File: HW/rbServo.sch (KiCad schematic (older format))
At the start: 8 parts, among them P101 EXTCON, P104 p5V, P105 pGND, P109 pA, P113 M+, P114 M-

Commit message: Trying new layout
Signed-off-by: RasmusB <RasmusB@users.noreply.github.com>
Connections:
- net CAN_HIGH: now also P101.3 (P3); no longer P101.2 (P2)
- net CAN_LOW: now also P101.2 (P2); no longer P101.3 (P3)
- net GND: now also P101.4 (P4); no longer P101.1 (P1)
- net uIn: now also P101.1 (P1); no longer P101.4 (P4)
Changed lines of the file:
@@
 F 3 "" H 3800 3550 60  0001 C CNN
 	1    3800 3550
-	-1   0    0    1
+	-1   0    0    -1
 $EndComp
 Text Label 7300 4400 2    60   ~ 0

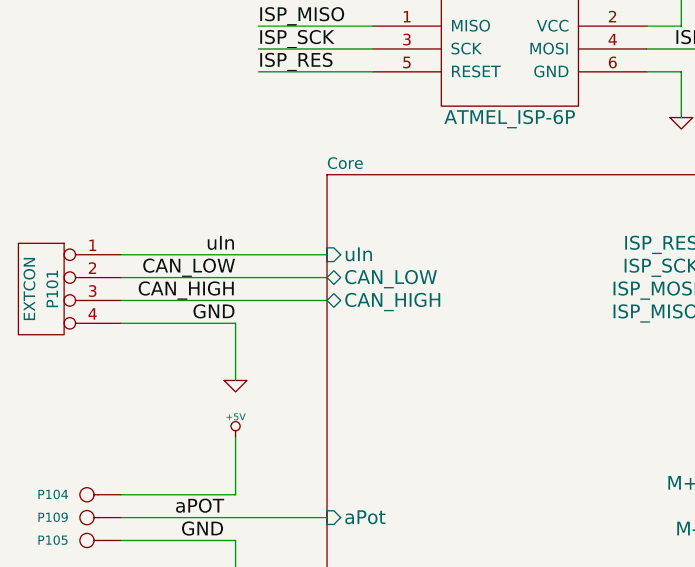
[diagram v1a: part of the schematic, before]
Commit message: -Swapped CAN_H and CAN_L -Changed a few labels - All new layout that should fit i a servo
Signed-off-by: RasmusB <RasmusB@users.noreply.github.com>
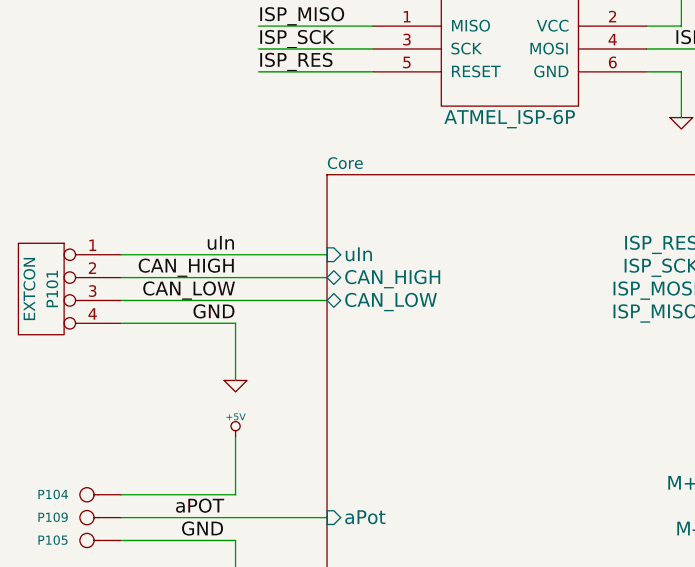
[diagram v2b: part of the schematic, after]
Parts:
- P104: value p5V -> 5V
- P105: value pGND -> GND
- P109: value pA -> Pot
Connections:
- net CAN_HIGH: now also P101.2 (P2); no longer P101.3 (P3)
- net CAN_LOW: now also P101.3 (P3); no longer P101.2 (P2)
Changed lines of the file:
@@
 	1    0    0    -1
 $EndComp
+Text Label 4650 3600 2    60   ~ 0
+CAN_LOW
 Text Label 4650 3500 2    60   ~ 0
-CAN_LOW
-Text Label 4650 3600 2    60   ~ 0
 CAN_HIGH
 Text Label 4750 2600 0    60   ~ 0
@@
 F6 "ISP_MOSI" I R 6750 3550 60
 F7 "ISP_SCK" I R 6750 3450 60
-F8 "CAN_HIGH" B L 5050 3600 60
-F9 "CAN_LOW" B L 5050 3500 60
+F8 "CAN_HIGH" B L 5050 3500 60
+F9 "CAN_LOW" B L 5050 3600 60
 F10 "ISP_RES" I R 6750 3350 60
 F11 "uIn" I L 5050 3400 60
@@
 P 4000 4450
 F 0 "P104" H 4080 4450 40  0000 L CNN
-F 1 "p5V" H 4000 4505 30  0001 C CNN
+F 1 "5V" H 4000 4505 30  0001 C CNN
 F 2 "" H 4000 4450 60  0000 C CNN
 F 3 "" H 4000 4450 60  0000 C CNN
@@
 P 4000 4650
 F 0 "P105" H 4080 4650 40  0000 L CNN
-F 1 "pGND" H 4000 4705 30  0001 C CNN
+F 1 "GND" H 4000 4705 30  0001 C CNN
 F 2 "" H 4000 4650 60  0000 C CNN
 F 3 "" H 4000 4650 60  0000 C CNN
@@
 P 4000 4550
 F 0 "P109" H 4080 4550 40  0000 L CNN
-F 1 "pA" H 4000 4605 30  0001 C CNN
+F 1 "Pot" H 4000 4605 30  0001 C CNN
 F 2 "" H 4000 4550 60  0000 C CNN
 F 3 "" H 4000 4550 60  0000 C CNN
